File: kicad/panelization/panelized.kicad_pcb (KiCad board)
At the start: 2 copper layers, 281.8 x 99.1 mm, 179 parts, among them J1 JST BATTERY R, J2 JST BATTERY R, SW1 SW_Push, SW10 SW_Push, SW11 SW_Push, SW12 SW_Push, SW13 SW_Push, SW14 SW_Push, SW15 SW_Push, SW16 SW_Push, SW17 SW_Push, SW18 SW_Push, SW19 SW_Push, SW2 SW_Push, SW20 SW_Push, SW21 SW_Push, SW22 SW_Push, SW23 SW_Push, SW24 SW_Push, SW25 SW_Push, SW26 SW_Push, SW27 SW_Push, SW28 SW_Push, SW29 SW_Push, SW3 SW_Push, SW30 SW_Push, SW31 SW_Push, SW32 SW_Push, SW33 SW_Push, SW34 SW_Push, SW35 SW_Push, SW36 SW_Push, SW37 SW_Push, SW38 SW_Push, SW39 SW_Push, SW4 SW_Push, SW40 SW_Push, SW41 SW_Push, SW42 SW_Push, SW5 SW_Push, SW6 SW_Push, SW7 SW_Push, SW8 SW_Push, SW9 SW_Push, U1 nice_nano, U2 nice_nano

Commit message: chore: move jst to allow room for 1.75u keycaps
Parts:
- moved J1 4.39 mm to (192.2, 78.1)
- moved J2 3.46 mm to (159.5, 78.1)
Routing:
- net Board_0-RBATTERY_POSITIVE: track 15.9 -> 13.6 mm
- net Board_0-LBATTERY_POSITIVE: track 9.33 -> 8.26 mm

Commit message: feat: use same cutout for both halves
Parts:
- moved KiKit_FID_B_3 0.39 mm to (39.5, 116.7)
- moved KiKit_FID_T_3 0.39 mm to (39.5, 116.7)
- moved KiKit_TO_3 0.39 mm to (37.0, 116.7)
- moved D13 0.37 mm to (130.7, 44.5)
- moved D14 0.37 mm to (130.7, 62.7)
- moved D15 0.37 mm to (130.7, 82.6)
- moved D16 0.37 mm to (149.7, 46.1)
- moved D17 0.37 mm to (150.0, 65.1)
- moved D18 0.37 mm to (144.0, 70.8)
- moved D19 0.37 mm to (313.9, 48.4)
- moved D20 0.37 mm to (313.9, 67.4)
- moved D21 0.37 mm to (313.9, 87.6)
- moved D22 0.37 mm to (294.9, 48.4)
- moved D23 0.37 mm to (294.9, 67.4)
- moved D24 0.37 mm to (294.9, 86.7)
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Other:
- board size 281.8 x 99.1 mm -> 281.1 x 99.2 mm
- board text added: "Created on 2025-04-04 JLC Order: JLCJLCJLC"
- board text removed: "Created on 2025-03-31 JLC Order: JLCJLCJLC"

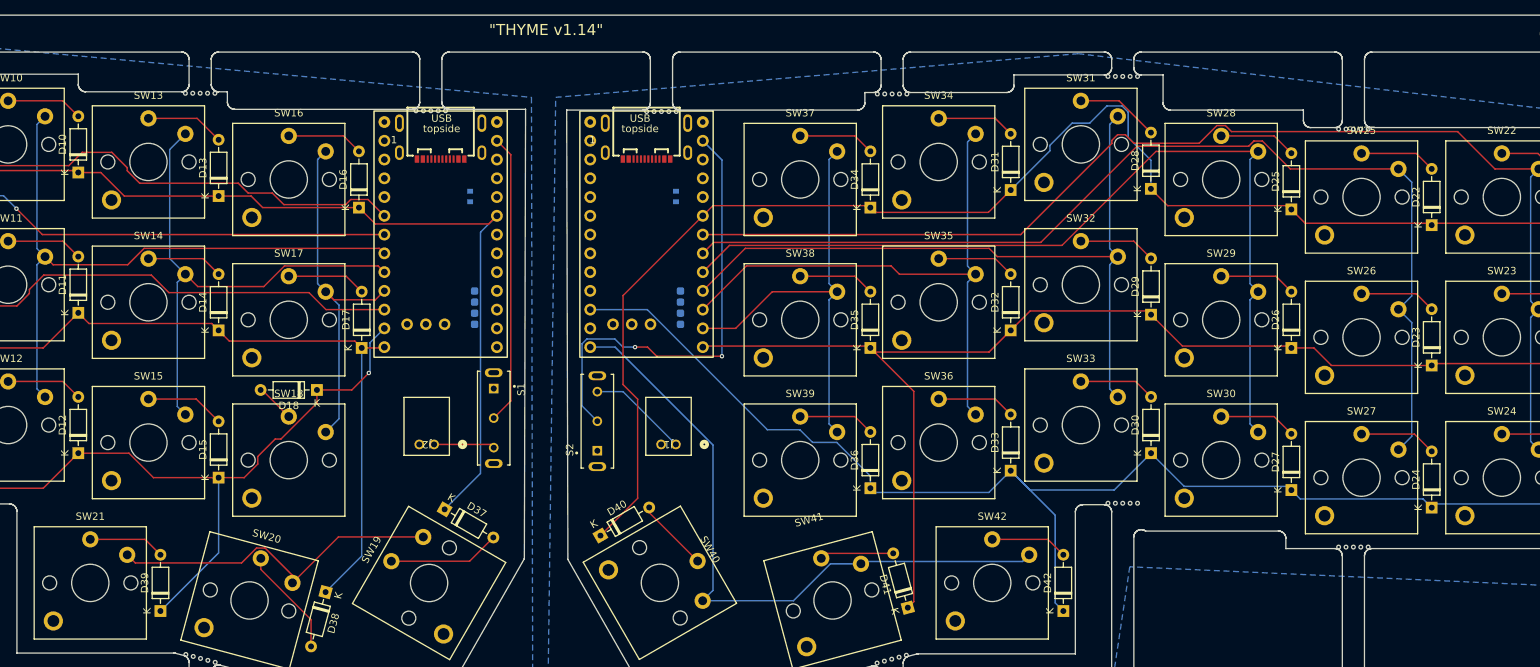
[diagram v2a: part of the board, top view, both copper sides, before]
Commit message: feat: use another row instead of col 7
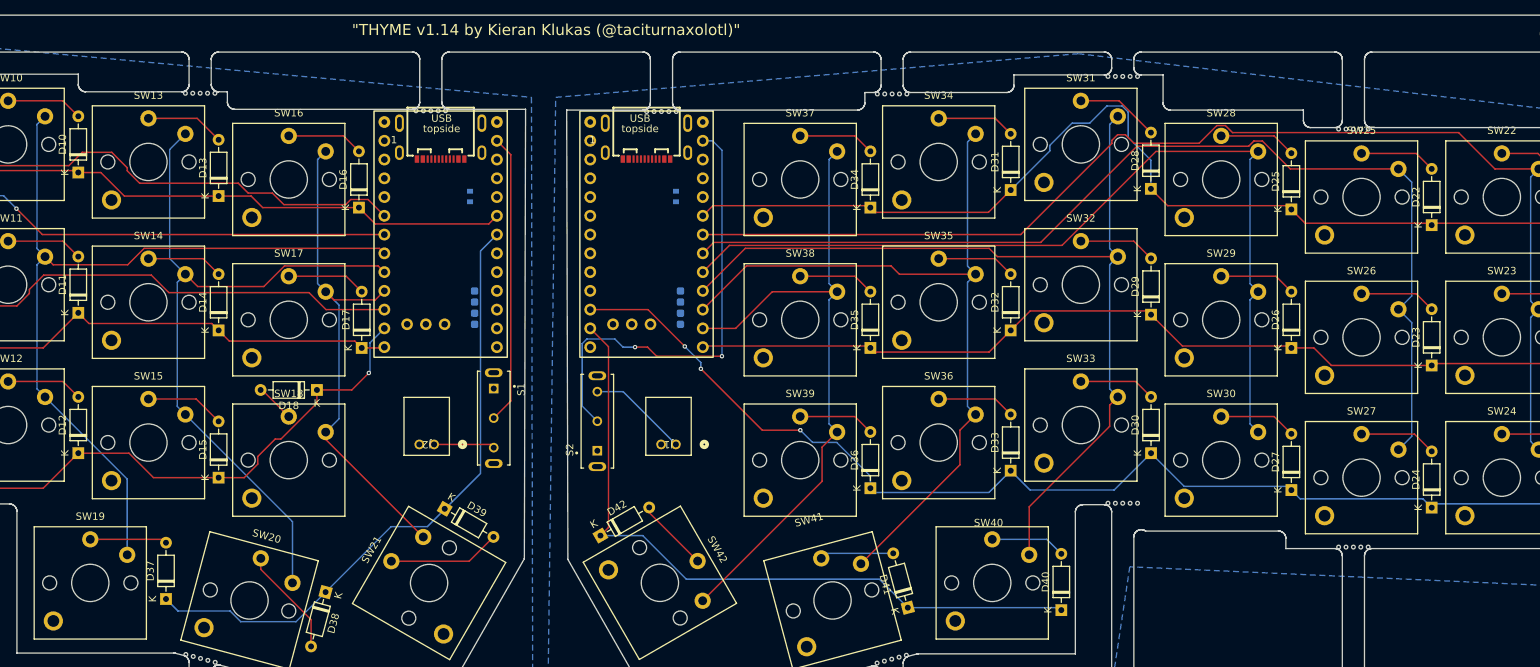
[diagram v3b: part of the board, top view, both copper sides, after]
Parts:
- moved D42 63.5 mm to (182.4, 90.5), turned to 30 degrees
- moved D40 63.2 mm to (244.8, 100.6), turned to 90 degrees
- moved SW19 45.9 mm to (113.3, 96.9), turned to 0 degrees
- moved SW21 45.9 mm to (159.2, 96.9), turned to 60 degrees
- moved SW40 45.0 mm to (235.4, 96.9), turned to 0 degrees
- moved SW42 45.0 mm to (190.4, 96.9), turned to -60 degrees
- moved D39 40.9 mm to (161.3, 86.8), turned to -30 degrees
- moved D37 39.6 mm to (123.5, 99.1), turned to 90 degrees
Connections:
- D37 pad 1: Board_0-L-ROW0 -> Board_0-L-ROW3
- D38 pad 1: Board_0-L-ROW1 -> Board_0-L-ROW3
- D39 pad 1: Board_0-L-ROW2 -> Board_0-L-ROW3
- D40 pad 1: Board_0-R-ROW0 -> Board_0-R-ROW3
- D41 pad 1: Board_0-R-ROW1 -> Board_0-R-ROW3
- D42 pad 1: Board_0-R-ROW2 -> Board_0-R-ROW3
- SW19 pad 2: Board_0-L-COL6 -> Board_0-L-COL3
- SW20 pad 2: Board_0-L-COL6 -> Board_0-L-COL4
- SW21 pad 2: Board_0-L-COL6 -> Board_0-L-COL5
- SW40 pad 2: Board_0-R-COL6 -> Board_0-R-COL3
- SW41 pad 2: Board_0-R-COL6 -> Board_0-R-COL4
- SW42 pad 2: Board_0-R-COL6 -> Board_0-R-COL5
- U1 pad 18: Board_0-unconnected-(U1-P0.29-LF-Pad18) -> Board_0-L-ROW3
- U2 pad 11: Board_0-unconnected-(U2-P1.04-LF-Pad11) -> Board_0-R-ROW3
- U2 pad 12: Board_0-R-COL6 -> Board_0-unconnected-(U2-P1.06-LF-Pad12)
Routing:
- net Board_0-R-ROW3: track 0.00 -> 96.1 mm
- net Board_0-R-COL6: track 90.6 -> 0.00 mm
- net Board_0-L-ROW3: track 0.00 -> 84.6 mm
- net Board_0-R-ROW0: track 186.9 -> 136.2 mm
- net Board_0-L-COL6: track 46.5 -> 0.00 mm
- net Board_0-L-ROW0: track 166.0 -> 123.3 mm
- net Board_0-R-ROW1: track 161.6 -> 123.7 mm
- net Board_0-L-ROW1: track 139.2 -> 104.1 mm
- net Board_0-R-COL5: track 60.1 -> 90.5 mm
- net Board_0-L-COL4: track 69.8 -> 98.6 mm
- net Board_0-R-COL4: track 79.7 -> 106.3 mm
- net Board_0-R-COL3: track 98.9 -> 125.2 mm
- net Board_0-L-COL3: track 87.4 -> 113.4 mm
- net Board_0-R-ROW2: track 174.3 -> 153.0 mm, vias 0 -> 3
- net Board_0-L-ROW2: track 136.9 -> 115.6 mm
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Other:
- board text added: ""THYME v1.14 by Kieran Klukas (@taciturnaxolotl)""
- board text removed: ""THYME v1.14""

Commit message: feat: redesign edge cuts and key spacing
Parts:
- added KiKit_MB_10_6: NPTH, NPTH, F.Cu at (90.2, 98.7)
- added KiKit_MB_10_7: NPTH, NPTH, F.Cu at (89.6, 97.9)
- added KiKit_MB_12_6: NPTH, NPTH, F.Cu at (156.9, 102.8)
- added KiKit_MB_12_7: NPTH, NPTH, F.Cu at (156.3, 103.8)
- added KiKit_MB_13_6: NPTH, NPTH, F.Cu at (190.8, 99.2)
- added KiKit_MB_13_7: NPTH, NPTH, F.Cu at (190.2, 98.2)
- added KiKit_MB_15_6: NPTH, NPTH, F.Cu at (257.4, 102.5)
- added KiKit_MB_15_7: NPTH, NPTH, F.Cu at (256.8, 103.3)
- SW21, SW42: footprint Switch_Keyboard_Kailh:SW_Kailh_Choc_V1V2_1.00u -> Switch_Keyboard_Kailh:SW_Kailh_Choc_V1V2_1.50u
- moved KiKit_MB_10_1 17.8 mm to (93.2, 102.9)
- moved KiKit_MB_15_5 17.0 mm to (258.0, 101.6)
- moved KiKit_MB_10_2 16.9 mm to (92.6, 102.0)
- moved KiKit_MB_15_4 16.1 mm to (258.6, 100.8)
- moved KiKit_MB_10_3 16.0 mm to (92.0, 101.2)
- moved KiKit_MB_15_3 15.2 mm to (259.2, 100.0)
- moved KiKit_MB_10_4 15.1 mm to (91.4, 100.4)
- moved KiKit_MB_15_2 14.2 mm to (259.8, 99.1)
- moved KiKit_MB_10_5 14.1 mm to (90.8, 99.5)
- moved KiKit_MB_15_1 13.3 mm to (260.4, 98.3)
- moved KiKit_MB_12_1 12.2 mm to (159.8, 97.8)
- moved KiKit_MB_12_2 11.2 mm to (159.2, 98.8)
- moved KiKit_FID_B_3 10.7 mm to (29.3, 119.8)
- moved KiKit_FID_T_3 10.7 mm to (29.3, 119.8)
- moved KiKit_TO_3 10.7 mm to (26.8, 119.8)
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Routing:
- net Board_0-Net-(S2-Pad2): track 62.5 -> 56.9 mm
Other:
- board size 281.1 x 99.2 mm -> 301.5 x 102.3 mm
- board text added: ""THYME v1.16""
- board text added: "Created on 2025-04-10 JLC Order: JLCJLCJLC"
- board text removed: ""THYME v1.14 by Kieran Klukas (@taciturnaxolotl)""
- board text removed: "Created on 2025-04-04 JLC Order: JLCJLCJLC"

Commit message: feat: add stabilizers
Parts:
- SW1, SW10, SW11, SW12, SW13, SW14, SW15, SW16, SW17, SW18, SW19, SW2, SW20, SW22, SW23, SW24, SW25, SW26, SW27, SW28, SW29, SW3, SW30, SW31, SW32, SW33, SW34, SW35, SW36, SW37, SW38, SW39, SW4, SW40, SW41, SW5, SW6, SW7, SW8, SW9: footprint Switch_Keyboard_Kailh:SW_Kailh_Choc_V1V2_1.00u -> PCM_Switch_Keyboard_Hotswap_Kailh:SW_Hotswap_Kailh_Choc_V1V2_1.00u
- SW21, SW42: footprint Switch_Keyboard_Kailh:SW_Kailh_Choc_V1V2_1.50u -> PCM_Switch_Keyboard_Hotswap_Kailh:SW_Hotswap_Kailh_Choc_V1V2_1.00u
- moved D37 5.40 mm to (114.3, 104.3)
- moved D1 4.02 mm to (45.4, 51.9)
- moved D12 3.77 mm to (102.4, 83.0)
- moved D9 3.77 mm to (83.4, 87.7)
- moved D22 3.64 mm to (304.4, 52.4)
- moved D38 3.59 mm to (135.1, 101.5)
- moved D11 3.56 mm to (102.4, 63.7)
- moved D4 3.56 mm to (64.4, 51.9)
- moved D41 3.56 mm to (234.4, 104.0)
- moved D26 3.55 mm to (285.6, 68.9)
- moved D23 3.49 mm to (304.5, 71.3)
- moved D19 3.46 mm to (323.5, 52.2)
- moved D35 3.43 mm to (228.4, 68.8)
- moved D36 3.42 mm to (228.4, 87.8)
- moved D20 3.42 mm to (323.6, 71.2)
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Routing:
- net Board_0-R-COL3: track 125.2 -> 144.9 mm, vias 0 -> 2
- net Board_0-R-COL4: track 106.3 -> 124.3 mm, vias 0 -> 1
- net Board_0-R-COL5: track 90.5 -> 104.1 mm, vias 0 -> 1
- net Board_0-R-ROW0: track 136.2 -> 124.2 mm
- net Board_0-R-COL2: track 121.8 -> 133.8 mm, vias 0 -> 1
- net Board_0-R-COL0: track 162.8 -> 172.5 mm, vias 0 -> 1
- net Board_0-L-ROW3: track 84.6 -> 92.9 mm
- net Board_0-L-COL0: track 150.5 -> 142.7 mm
- net Board_0-L-COL1: track 128.6 -> 121.1 mm, vias 2 -> 1
- net Board_0-L-COL5: track 69.0 -> 62.4 mm
- net Board_0-Net-(D37-A): track 10.4 -> 16.2 mm
- net Board_0-Net-(D38-A): track 14.7 -> 20.2 mm
- net Board_0-L-COL4: track 98.6 -> 93.2 mm, vias 0 -> 1
- net Board_0-Net-(D1-A): track 10.2 -> 15.4 mm
- net Board_0-Net-(D9-A): track 10.4 -> 15.5 mm
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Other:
- board size 301.5 x 102.3 mm -> 301.4 x 102.3 mm
- board text added: ""THYME v1.17""
- board text removed: ""THYME v1.16""

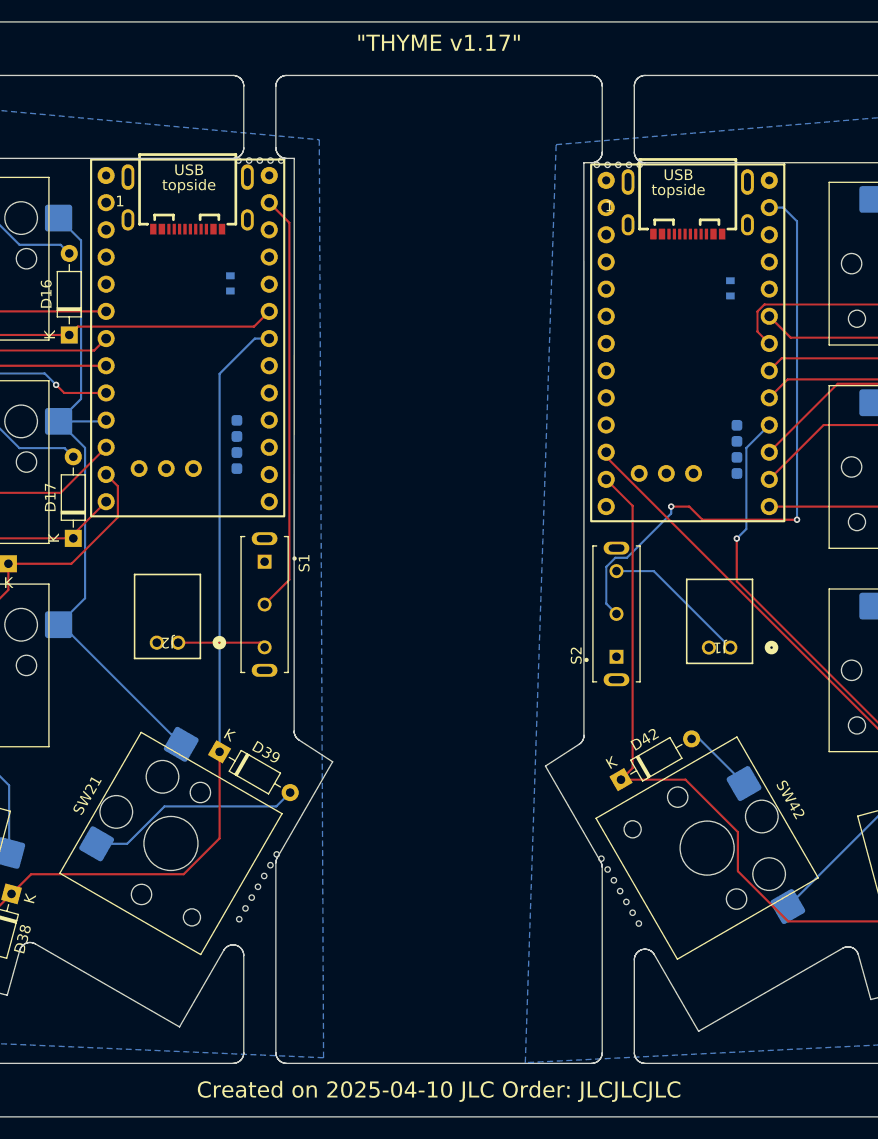
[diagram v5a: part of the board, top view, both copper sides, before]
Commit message: feat: remove uncessessary bits of footprint
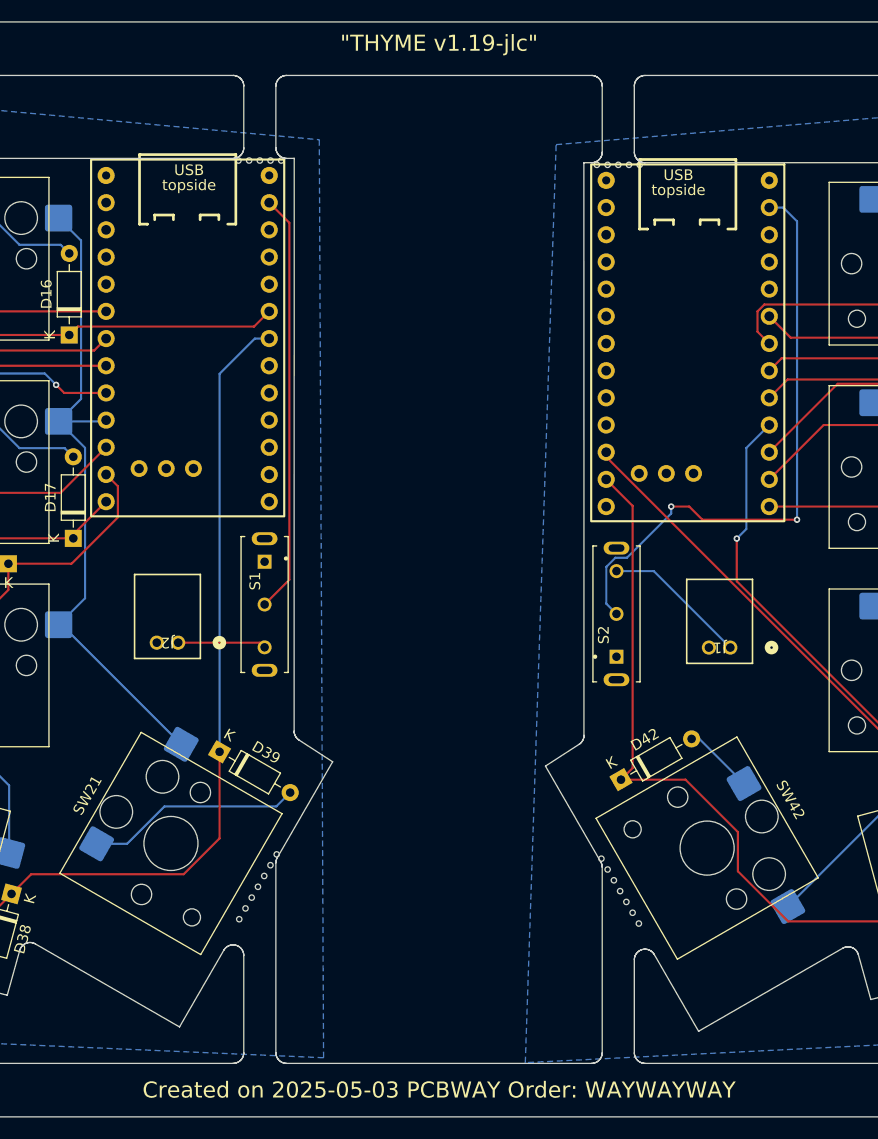
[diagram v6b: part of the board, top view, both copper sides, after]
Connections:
- net Board_0-unconnected-(U1-P0.06-Pad1)_1 renamed Board_0-unconnected-(U1-P0.06-Pad1)
- net Board_0-unconnected-(U1-P0.08-Pad2)_1 renamed Board_0-unconnected-(U1-P0.08-Pad2)
- net Board_0-unconnected-(U1-RST-Pad15)_1 renamed Board_0-unconnected-(U1-RST-Pad15)
- net Board_0-unconnected-(U2-P0.06-Pad1)_1 renamed Board_0-unconnected-(U2-P0.06-Pad1)
- net Board_0-unconnected-(U2-P0.08-Pad2) renamed Board_0-unconnected-(U2-P0.08-Pad2)_1
- net Board_0-unconnected-(U2-RST-Pad15) renamed Board_0-unconnected-(U2-RST-Pad15)_1
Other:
- board text added: ""THYME v1.19-jlc""
- board text added: "Created on 2025-05-03 PCBWAY Order: WAYWAYWAY"
- board text removed: ""THYME v1.17""
- board text removed: "Created on 2025-04-10 JLC Order: JLCJLCJLC"
